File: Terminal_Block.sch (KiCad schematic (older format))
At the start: 0 parts

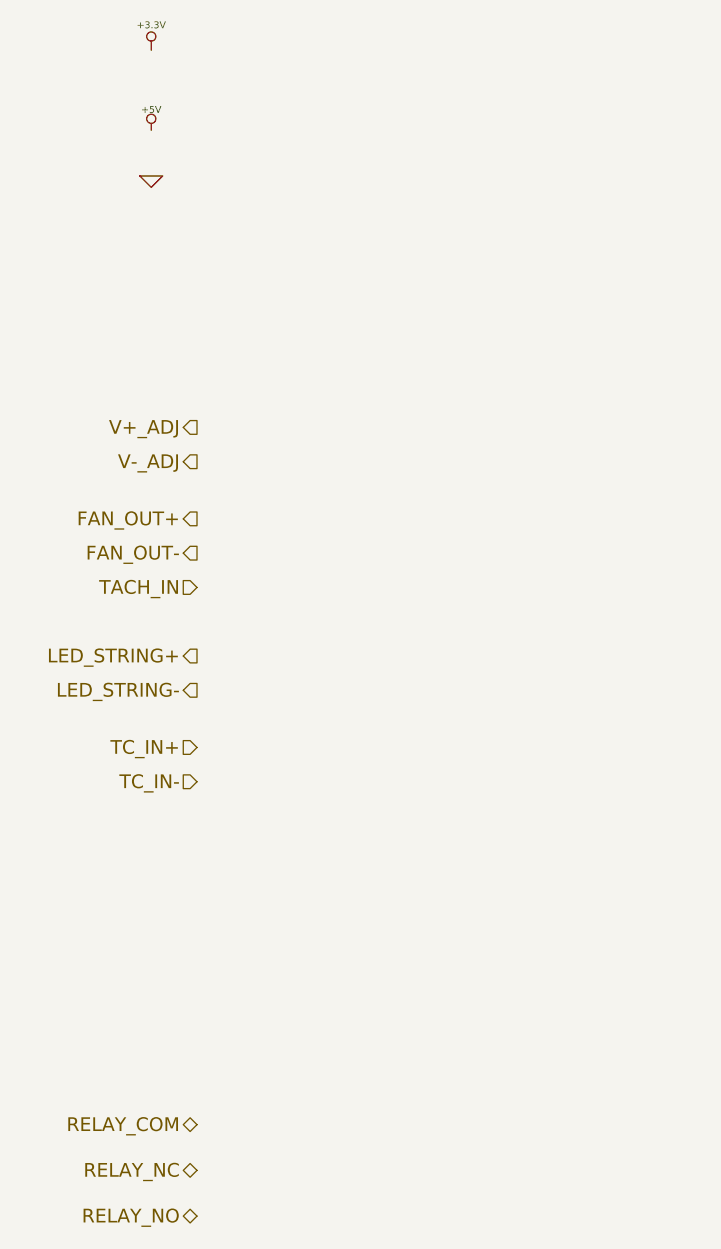
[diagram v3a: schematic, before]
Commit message: Associating and Placing the Terminal/ATX Blocks
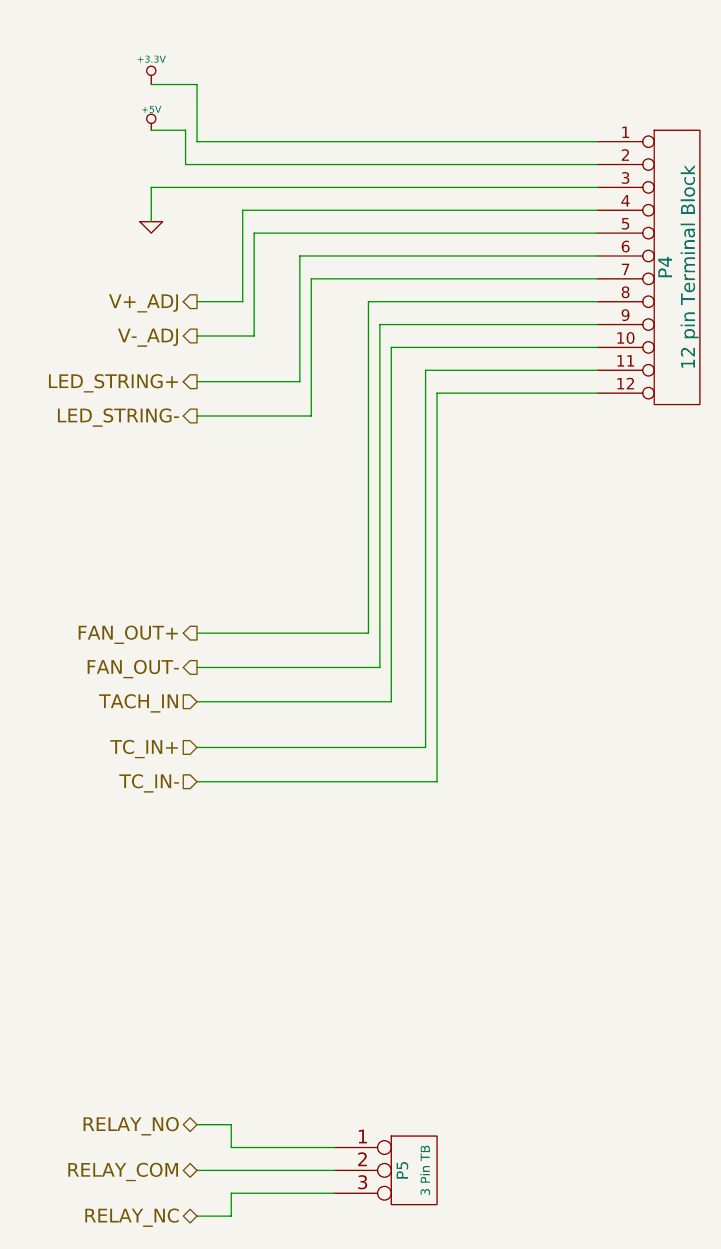
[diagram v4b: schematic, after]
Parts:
- added P4: 12 pin Terminal Block, symbol CONN_12
- added P5: 3 Pin TB, symbol CONN_3
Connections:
- net +3.3V: now also P4.1 (P1)
- net +5V: now also P4.2 (P2)
- net FAN_OUT+: now also P4.8 (P8)
- net FAN_OUT-: now also P4.9 (P9)
- net GND: now also P4.3 (P3)
- net LED_STRING+: now also P4.6 (P6)
- net LED_STRING-: now also P4.7 (P7)
- net RELAY_COM: now also P5.2 (PM)
- net RELAY_NC: now also P5.3 (P3)
- net RELAY_NO: now also P5.1 (P1)
- net TACH_IN: now also P4.10 (P10)
- net TC_IN+: now also P4.11 (P11)
- net TC_IN-: now also P4.12 (P12)
- net V+_ADJ: now also P4.4 (P4)
- net V-_ADJ: now also P4.5 (P5)
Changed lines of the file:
@@
 Comment4 ""
 $EndDescr
-Text HLabel 2000 2600 0    60   Output ~ 0
+Text HLabel 2000 2050 0    60   Output ~ 0
 V+_ADJ
-Text HLabel 2000 2750 0    60   Output ~ 0
+Text HLabel 2000 2200 0    60   Output ~ 0
 V-_ADJ
-Text HLabel 2000 3000 0    60   Output ~ 0
+Text HLabel 2000 3500 0    60   Output ~ 0
 FAN_OUT+
-Text HLabel 2000 3150 0    60   Output ~ 0
+Text HLabel 2000 3650 0    60   Output ~ 0
 FAN_OUT-
-Text HLabel 2000 3300 0    60   Input ~ 0
+Text HLabel 2000 3800 0    60   Input ~ 0
 TACH_IN
-Text HLabel 2000 3600 0    60   Output ~ 0
+Text HLabel 2000 2400 0    60   Output ~ 0
 LED_STRING+
-Text HLabel 2000 3750 0    60   Output ~ 0
+Text HLabel 2000 2550 0    60   Output ~ 0
 LED_STRING-
 Text HLabel 2000 4000 0    60   Input ~ 0
@@
 Text HLabel 2000 4150 0    60   Input ~ 0
 TC_IN-
+Text HLabel 2000 6050 0    60   BiDi ~ 0
+RELAY_NC
+Text HLabel 2000 5650 0    60   BiDi ~ 0
+RELAY_NO
 Text HLabel 2000 5850 0    60   BiDi ~ 0
-RELAY_NC
-Text HLabel 2000 6050 0    60   BiDi ~ 0
-RELAY_NO
-Text HLabel 2000 5650 0    60   BiDi ~ 0
 RELAY_COM
 $Comp
 L +3.3V #PWR032
 U 1 1 52F47434
-P 1800 950
-F 0 "#PWR032" H 1800 910 30  0001 C CNN
-F 1 "+3.3V" H 1800 1060 30  0000 C CNN
-F 2 "" H 1800 950 60  0000 C CNN
-F 3 "" H 1800 950 60  0000 C CNN
-	1    1800 950
+P 1800 1100
+F 0 "#PWR032" H 1800 1060 30  0001 C CNN
+F 1 "+3.3V" H 1800 1210 30  0000 C CNN
+F 2 "" H 1800 1100 60  0000 C CNN
+F 3 "" H 1800 1100 60  0000 C CNN
+	1    1800 1100
 	1    0    0    -1
 $EndComp
@@
 L GND #PWR034
 U 1 1 52F47470
-P 1800 1500
-F 0 "#PWR034" H 1800 1500 30  0001 C CNN
-F 1 "GND" H 1800 1430 30  0001 C CNN
-F 2 "" H 1800 1500 60  0000 C CNN
-F 3 "" H 1800 1500 60  0000 C CNN
-	1    1800 1500
+P 1800 1700
+F 0 "#PWR034" H 1800 1700 30  0001 C CNN
+F 1 "GND" H 1800 1630 30  0001 C CNN
+F 2 "" H 1800 1700 60  0000 C CNN
+F 3 "" H 1800 1700 60  0000 C CNN
+	1    1800 1700
 	1    0    0    -1
 $EndComp
+$Comp
+L CONN_12 P4
+U 1 1 53056460
+P 4100 1900
+F 0 "P4" V 4050 1900 60  0000 C CNN
+F 1 "12 pin Terminal Block" V 4150 1900 60  0000 C CNN
+F 2 "" H 4100 1900 60  0000 C CNN
+F 3 "" H 4100 1900 60  0000 C CNN
+F 4 "On Shore Technology Inc" H 4100 1900 60  0001 C CNN "MFG Name"
+F 5 "OSTTE120104" H 4100 1900 60  0001 C CNN "MFG Part Number"
+	1    4100 1900
+	1    0    0    -1
+$EndComp
+Wire Wire Line
+	1800 1100 2000 1100
+Wire Wire Line
+	2000 1350 3750 1350
+Wire Wire Line
+	1800 1300 1950 1300
+Wire Wire Line
+	1950 1300 1950 1450
+Wire Wire Line
+	1950 1450 3750 1450
+Wire Wire Line
+	1800 1700 1800 1550
+Wire Wire Line
+	1800 1550 3750 1550
+Wire Wire Line
+	2000 2050 2200 2050
+Wire Wire Line
+	2200 2050 2200 1650
+Wire Wire Line
+	2200 1650 3750 1650
+Wire Wire Line
+	3750 1750 2250 1750
+Wire Wire Line
+	2250 1750 2250 2200
+Wire Wire Line
+	2250 2200 2000 2200
+Wire Wire Line
+	2000 2400 2450 2400
+Wire Wire Line
+	2450 2400 2450 1850
+Wire Wire Line
+	2450 1850 3750 1850
+Wire Wire Line
+	2000 2550 2500 2550
+Wire Wire Line
+	2500 2550 2500 1950
+Wire Wire Line
+	2500 1950 3750 1950
+Wire Wire Line
+	2000 3500 2750 3500
+Wire Wire Line
+	2750 3500 2750 2050
+Wire Wire Line
+	2750 2050 3750 2050
+Wire Wire Line
+	3750 2150 2800 2150
+Wire Wire Line
+	2800 2150 2800 3650
+Wire Wire Line
+	2800 3650 2000 3650
+Wire Wire Line
+	2000 3800 2850 3800
+Wire Wire Line
+	2850 3800 2850 2250
+Wire Wire Line
+	2850 2250 3750 2250
+Wire Wire Line
+	3750 2350 3000 2350
+Wire Wire Line
+	3000 2350 3000 4000
+Wire Wire Line
+	3000 4000 2000 4000
+Wire Wire Line
+	2000 4150 3050 4150
+Wire Wire Line
+	3050 4150 3050 2450
+Wire Wire Line
+	3050 2450 3750 2450
+Wire Wire Line
+	2000 1100 2000 1350
+$Comp
+L CONN_3 P5
+U 1 1 5305685C
+P 2950 5850
+F 0 "P5" V 2900 5850 50  0000 C CNN
+F 1 "3 Pin TB" V 3000 5850 40  0000 C CNN
+F 2 "" H 2950 5850 60  0000 C CNN
+F 3 "" H 2950 5850 60  0000 C CNN
+F 4 "Phoenix" H 2950 5850 60  0001 C CNN "MFG Name"
+F 5 "1935174" H 2950 5850 60  0001 C CNN "MFG Part Number"
+	1    2950 5850
+	1    0    0    -1
+$EndComp
+Wire Wire Line
+	2600 5750 2150 5750
+Wire Wire Line
+	2150 5750 2150 5650
+Wire Wire Line
+	2150 5650 2000 5650
+Wire Wire Line
+	2000 5850 2600 5850
+Wire Wire Line
+	2600 5950 2150 5950
+Wire Wire Line
+	2150 5950 2150 6050
+Wire Wire Line
+	2150 6050 2000 6050
 $EndSCHEMATC
